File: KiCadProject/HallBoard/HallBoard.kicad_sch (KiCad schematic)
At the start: 6 parts, among them J101 JST_SM04B, J102 JST_SM04B, U101 TLE493D

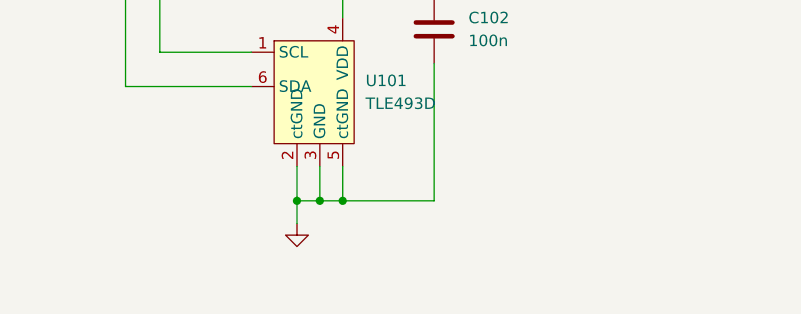
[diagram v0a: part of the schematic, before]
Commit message: Components selected, MfID added to schematics, and components ordered
Signed-off-by: Eldalote.Electronics <Eldalote.Electronics@gmail.com>
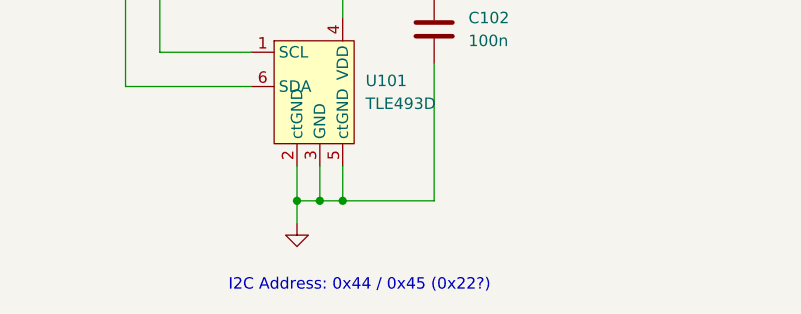
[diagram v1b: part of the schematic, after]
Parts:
- C101, C103: MfID (none) -> CL10A105KA8NNNC
- C102: MfID (none) -> CL05A104KA5NNNC
- J101, J102: MfID (none) -> SM04B-SRSS-TB(LF)(SN)
- U101: MfID (none) -> TLE493DW2B6A1HTSA1
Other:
- note added: "I2C Address: 0x44 / 0x45 (0x22?)"
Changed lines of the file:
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@@
     (stroke (width 0) (type default) (color 0 0 0 0))
+  )
+  (text "I2C Address: 0x44 / 0x45 (0x22?)" (at 129.54 137.16 0)
+    (effects (font (size 1.27 1.27)) (justify left bottom))
   )
   (label "I2C_SCL" (at 137.16 77.47 0)
@@
       (effects (font (size 1.27 1.27)) hide)
     )
+    (property "MfID" "CL10A105KA8NNNC" (id 4) (at 93.98 67.31 0)
+      (effects (font (size 1.27 1.27)) hide)
+    )
     (pin "1")
     (pin "2")
@@
     )
     (property "Datasheet" "~" (id 3) (at 175.26 74.93 0)
+      (effects (font (size 1.27 1.27)) hide)
+    )
+    (property "MfID" "SM04B-SRSS-TB(LF)(SN)" (id 4) (at 175.26 74.93 0)
       (effects (font (size 1.27 1.27)) hide)
     )
@@
       (effects (font (size 1.27 1.27)) hide)
     )
+    (property "MfID" "SM04B-SRSS-TB(LF)(SN)" (id 4) (at 99.06 74.93 0)
+      (effects (font (size 1.27 1.27)) hide)
+    )
     (pin "1")
     (pin "2")
@@
       (effects (font (size 1.27 1.27)) hide)
     )
+    (property "MfID" "CL05A104KA5NNNC" (id 4) (at 152.4 107.95 0)
+      (effects (font (size 1.27 1.27)) hide)
+    )
     (pin "1")
     (pin "2")
@@
       (effects (font (size 1.27 1.27)) hide)
     )
+    (property "MfID" "CL10A105KA8NNNC" (id 4) (at 181.61 67.31 0)
+      (effects (font (size 1.27 1.27)) hide)
+    )
     (pin "1")
     (pin "2")
@@
       (effects (font (size 1.27 1.27)) hide)
     )
+    (property "MfID" "TLE493DW2B6A1HTSA1" (id 4) (at 139.7 115.57 0)
+      (effects (font (size 1.27 1.27)) hide)
+    )

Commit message: Made ready to order PCBs. Some problems with ordering due to misunderstanding. Thinking about solutions
Signed-off-by: Eldalote.Electronics <Eldalote.Electronics@gmail.com>
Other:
- company: (none) -> Eldalote Electronics
- title: (none) -> Hall Sensor for outside interaction
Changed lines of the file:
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@@
 (kicad_sch (version 20211123) (generator eeschema)
   (paper "A4")
+  (title_block
+    (title "Hall Sensor for outside interaction")
+    (date "2023-02-02")
+    (rev "0.1")
+    (company "Eldalote Electronics")
+    (comment 2 "Part of the Dive lamp design")
+  )
   (junction (at 139.7 127) (diameter 0) (color 0 0 0 0)
   )
